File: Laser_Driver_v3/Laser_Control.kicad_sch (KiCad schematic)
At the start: 10 parts, among them U30 74AHCT125, U31 AD9833xRM, U32 AD5064BRUZ, U33 AD9833xRM

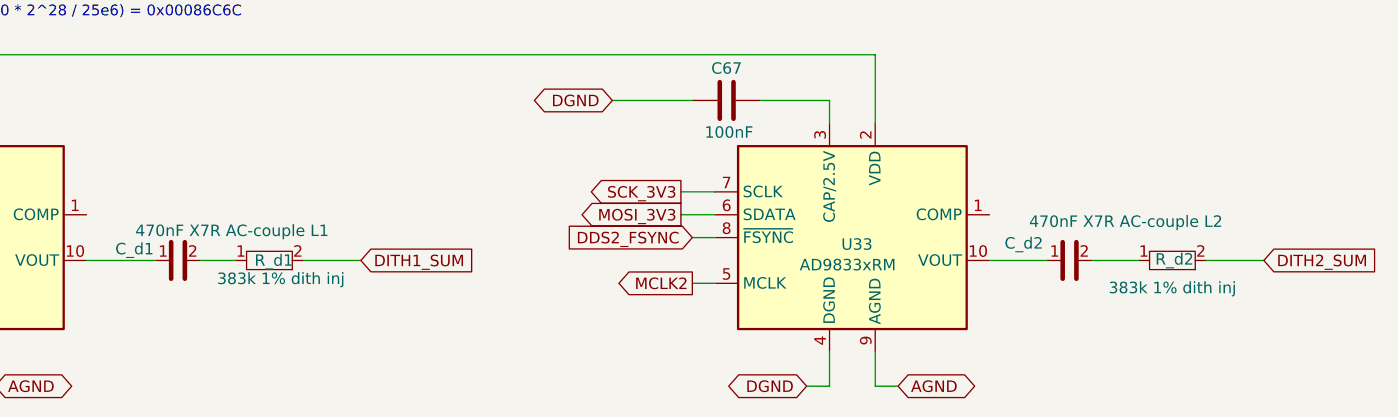
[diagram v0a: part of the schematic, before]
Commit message: Update names, footprints, values, and created BOM
Updated files names, foot prints, component values, parts.
Assigned values from Digikey catalog.
Created CSV BOMs for each schematic.
Including a Power analysis now for all components.
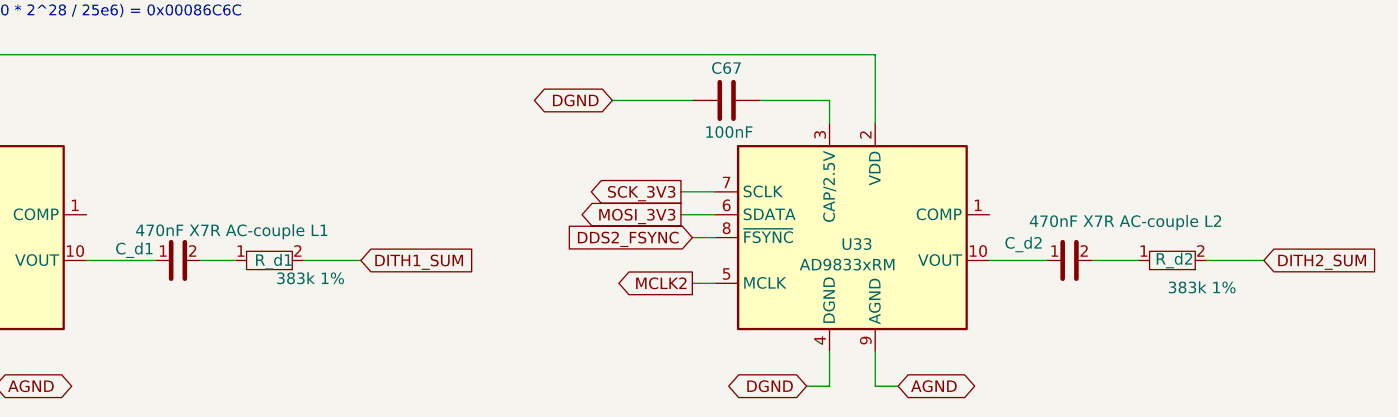
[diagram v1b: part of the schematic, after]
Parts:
- C_d1, C_d2: footprint Capacitor_SMD:C_0805_2012Metric -> Capacitor_SMD:C_0805_2012Metric_Pad1.18x1.45mm_HandSolder
- R_d1, R_d2: value 383k 1% dith inj -> 383k 1%; footprint Resistor_SMD:R_0402_1005Metric -> Resistor_SMD:R_0805_2012Metric_Pad1.20x1.40mm_HandSolder
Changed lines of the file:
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@@
 			)
 		)
-		(property "Footprint" "Capacitor_SMD:C_0805_2012Metric"
+		(property "Footprint" "Capacitor_SMD:C_0805_2012Metric_Pad1.18x1.45mm_HandSolder"
 			(at 86.36 143.51 0)
 			(hide yes)
@@
 			)
 		)
-		(property "Footprint" "Capacitor_SMD:C_0805_2012Metric"
+		(property "Footprint" "Capacitor_SMD:C_0805_2012Metric_Pad1.18x1.45mm_HandSolder"
 			(at 185.42 143.51 0)
 			(hide yes)
@@
 			)
 		)
-		(property "Value" "383k 1% dith inj"
+		(property "Value" "383k 1%"
 			(at 203.962 146.558 90)
 			(show_name no)
@@
 			)
 		)
-		(property "Footprint" "Resistor_SMD:R_0402_1005Metric"
+		(property "Footprint" "Resistor_SMD:R_0805_2012Metric_Pad1.20x1.40mm_HandSolder"
 			(at 196.85 143.51 0)
 			(hide yes)
@@
 			)
 		)
-		(property "Value" "383k 1% dith inj"
+		(property "Value" "383k 1%"
 			(at 104.902 145.542 90)
 			(show_name no)
@@
 			)
 		)
-		(property "Footprint" "Resistor_SMD:R_0402_1005Metric"
+		(property "Footprint" "Resistor_SMD:R_0805_2012Metric_Pad1.20x1.40mm_HandSolder"
 			(at 96.52 143.51 0)
 			(hide yes)

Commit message: Clearing ERC errors. laying out components.
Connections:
- no-connect marks 1 -> 3
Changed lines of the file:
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@@
+	)
+	(no_connect
+		(at 176.53 138.43)
 	)
 	(no_connect
 		(at 111.76 73.66)
 	)
+	(no_connect
+		(at 76.2 138.43)
+	)
 	(wire
 		(pts
@@
 	(wire
 		(pts
+			(xy 40.64 163.83) (xy 40.64 168.91)
+		)
+		(stroke
+			(width 0)
+			(type default)
+		)
+	)
+	(wire
+		(pts
 			(xy 44.45 62.23) (xy 44.45 43.18)
 		)
@@
 	(wire
 		(pts
+			(xy 29.21 91.44) (xy 36.83 91.44)
+		)
+		(stroke
+			(width 0)
+			(type default)
+		)
+	)
+	(wire
+		(pts
 			(xy 111.76 66.04) (xy 119.38 66.04)
 		)
@@
 	(wire
 		(pts
-			(xy 29.21 91.44) (xy 36.83 91.44)
-		)
-		(stroke
-			(width 0)
-			(type default)
-		)
-	)
-	(wire
-		(pts
 			(xy 66.04 59.69) (xy 69.85 59.69)
 		)
@@
 		(pts
 			(xy 30.48 59.69) (xy 50.8 59.69)
+		)
+		(stroke
+			(width 0)
+			(type default)
+		)
+	)
+	(wire
+		(pts
+			(xy 35.56 163.83) (xy 40.64 163.83)
 		)
 		(stroke
@@
 	)
 	(global_label "DGND"
-		(shape bidirectional)
+		(shape output)
 		(at 55.88 157.48 180)
 		(fields_autoplaced yes)
@@
 		)
 		(property "Intersheetrefs" "${INTERSHEET_REFS}"
-			(at 46.643 157.48 0)
+			(at 47.7543 157.48 0)
 			(hide yes)
 			(show_name no)
@@
 	)
 	(global_label "DGND"
-		(shape bidirectional)
+		(shape output)
 		(at 156.21 157.48 180)
 		(fields_autoplaced yes)
@@
 		)
 		(property "Intersheetrefs" "${INTERSHEET_REFS}"
-			(at 146.973 157.48 0)
+			(at 148.0843 157.48 0)
 			(hide yes)
 			(show_name no)
@@
 	)
 	(global_label "AGND"
-		(shape bidirectional)
+		(shape output)
 		(at 166.37 157.48 0)
 		(fields_autoplaced yes)
@@
 		)
 		(property "Intersheetrefs" "${INTERSHEET_REFS}"
-			(at 175.4256 157.48 0)
+			(at 174.3143 157.48 0)
 			(hide yes)
 			(show_name no)
@@
 		)
 	)
+	(global_label "DGND"
+		(shape input)
+		(at 35.56 163.83 180)
+		(fields_autoplaced yes)
+		(effects
+			(font
+				(size 1.27 1.27)
+			)
+			(justify right)
+		)
+		(property "Intersheetrefs" "${INTERSHEET_REFS}"
+			(at 27.4343 163.83 0)
+			(hide yes)
+			(show_name no)
+			(do_not_autoplace no)
+			(effects
+				(font
+					(size 1.27 1.27)
+				)
+				(justify right)
+			)
+		)
+	)
 	(global_label "DDS2_FSYNC"
 		(shape input)
@@
 	)
 	(global_label "AGND"
-		(shape bidirectional)
+		(shape input)
 		(at 29.21 91.44 180)
 		(fields_autoplaced yes)
@@
 		)
 		(property "Intersheetrefs" "${INTERSHEET_REFS}"
-			(at 20.1544 91.44 0)
+			(at 21.2657 91.44 0)
 			(hide yes)
 			(show_name no)
@@
 	)
 	(global_label "AGND"
-		(shape bidirectional)
+		(shape output)
 		(at 66.04 157.48 0)
 		(fields_autoplaced yes)
@@
 		)
 		(property "Intersheetrefs" "${INTERSHEET_REFS}"
-			(at 75.0956 157.48 0)
+			(at 73.9843 157.48 0)
 			(hide yes)
 			(show_name no)
@@
 	)
 	(symbol
+		(lib_name "AD9833xRM_1")
 		(lib_id "Interface:AD9833xRM")
 		(at 60.96 140.97 0)
@@
 		)
 		(property "Value" "383k 1%"
-			(at 104.902 145.542 90)
+			(at 99.314 146.558 90)
 			(show_name no)
 			(do_not_autoplace no)
@@
 		(property "Datasheet" ""
 			(at 96.52 143.51 0)
+			(hide yes)
 			(show_name no)
 			(do_not_autoplace no)
@@
 					(unit 1)
 				)
+			)
+		)
+	)
+	(symbol
+		(lib_id "power:GND")
+		(at 40.64 168.91 0)
+		(unit 1)
+		(body_style 1)
+		(exclude_from_sim no)
+		(in_bom yes)
+		(on_board yes)
+		(in_pos_files yes)
+		(dnp no)
+		(property "Reference" "#PWR032"
+			(at 40.64 175.26 0)
+			(hide yes)
+			(show_name no)
+			(do_not_autoplace no)
+			(effects
+				(font
+					(size 1.27 1.27)
+				)
+			)
+		)
+		(property "Value" "DGND"
+			(at 42.672 169.418 0)
+			(show_name no)
+			(do_not_autoplace no)
+			(effects
+				(font
+					(size 1.27 1.27)
+				)
+			)
+		)
+		(property "Footprint" ""
+			(at 40.64 168.91 0)
+			(hide yes)
+			(show_name no)
+			(do_not_autoplace no)
+			(effects
+				(font
+					(size 1.27 1.27)
+				)
+			)
+		)
+		(property "Datasheet" ""
+			(at 40.64 168.91 0)
+			(hide yes)
+			(show_name no)
+			(do_not_autoplace no)
+			(effects
+				(font
+					(size 1.27 1.27)
+				)
+			)
+		)
+		(property "Description" "Power symbol creates a global label with name \"GND\" , ground"
+			(at 40.64 168.91 0)
+			(hide yes)
+			(show_name no)
+			(do_not_autoplace no)
+			(effects
+				(font
+					(size 1.27 1.27)
+				)
+			)
+		)
+		(pin "1"
+		)
+		(instances
+			(project "laser_driver_v3"
+				(path "/b2c3d4e5-f6a7-8901-bcde-f12345678901/e4d7b089-62e9-414f-b4cc-abd1480c07cf"
+					(reference "#PWR032")
+					(unit 1)
+				)

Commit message: Added display to schematic.  Updated BOM.
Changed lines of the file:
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@@
 	)
 	(global_label "DDS2_FSYNC"
-		(shape input)
+		(shape output)
 		(at 143.51 140.97 180)
 		(fields_autoplaced yes)
@@
 		)
 		(property "Intersheetrefs" "${INTERSHEET_REFS}"
-			(at 143.51 140.97 0)
+			(at 128.611 140.97 0)
 			(hide yes)
 			(show_name no)

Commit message: Update to teensy pinout and config. Working on PCB
Improved pin selection on Teensy for better operation.
Started working through the PCB from in the power input.
Updating footprints and getting the layout organized.
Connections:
- net 5V_DAC: no longer U32.9 (~{CLR})
- net GND: no longer U30.11 (4Y), U30.12 (4A)
- new net: U30.11 (4Y), U32.9 (~{CLR})
- new net AD5064_CLR: U30.12 (4A)
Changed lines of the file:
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@@
-	)
-	(junction
-		(at 69.85 67.31)
-		(diameter 0)
-		(color 0 0 0 0)
 	)
 	(junction
@@
 	)
 	(junction
-		(at 69.85 64.77)
-		(diameter 0)
-		(color 0 0 0 0)
-	)
-	(junction
 		(at 69.85 57.15)
-		(diameter 0)
-		(color 0 0 0 0)
-	)
-	(junction
-		(at 95.25 63.5)
 		(diameter 0)
 		(color 0 0 0 0)
@@
 	(wire
 		(pts
-			(xy 69.85 67.31) (xy 71.12 67.31)
+			(xy 66.04 67.31) (xy 71.12 67.31)
 		)
 		(stroke
@@
 	(wire
 		(pts
+			(xy 76.2 86.36) (xy 76.2 64.77)
+		)
+		(stroke
+			(width 0)
+			(type default)
+		)
+	)
+	(wire
+		(pts
 			(xy 50.8 64.77) (xy 48.26 64.77)
 		)
@@
 	(wire
 		(pts
-			(xy 69.85 46.99) (xy 73.66 46.99)
-		)
-		(stroke
-			(width 0)
-			(type default)
-		)
-	)
-	(wire
-		(pts
-			(xy 80.01 86.36) (xy 80.01 62.23)
+			(xy 72.39 53.34) (xy 73.66 53.34)
 		)
 		(stroke
@@
 	(wire
 		(pts
-			(xy 95.25 62.23) (xy 95.25 63.5)
-		)
-		(stroke
-			(width 0)
-			(type default)
-		)
-	)
-	(wire
-		(pts
 			(xy 143.51 146.05) (xy 146.05 146.05)
 		)
@@
 	(wire
 		(pts
-			(xy 73.66 46.99) (xy 73.66 57.15)
-		)
-		(stroke
-			(width 0)
-			(type default)
-		)
-	)
-	(wire
-		(pts
-			(xy 80.01 62.23) (xy 95.25 62.23)
+			(xy 73.66 53.34) (xy 73.66 57.15)
+		)
+		(stroke
+			(width 0)
+			(type default)
+		)
+	)
+	(wire
+		(pts
+			(xy 74.93 46.99) (xy 74.93 62.23)
 		)
 		(stroke
@@
 	(wire
 		(pts
-			(xy 69.85 64.77) (xy 69.85 67.31)
-		)
-		(stroke
-			(width 0)
-			(type default)
-		)
-	)
-	(wire
-		(pts
 			(xy 114.3 43.18) (xy 114.3 58.42)
 		)
@@
 	(wire
 		(pts
-			(xy 66.04 67.31) (xy 69.85 67.31)
-		)
-		(stroke
-			(width 0)
-			(type default)
-		)
-	)
-	(wire
-		(pts
 			(xy 73.66 57.15) (xy 69.85 57.15)
 		)
@@
 	(wire
 		(pts
-			(xy 66.04 62.23) (xy 69.85 62.23)
+			(xy 66.04 62.23) (xy 74.93 62.23)
 		)
 		(stroke
@@
 	(wire
 		(pts
-			(xy 69.85 62.23) (xy 69.85 64.77)
-		)
-		(stroke
-			(width 0)
-			(type default)
-		)
-	)
-	(wire
-		(pts
 			(xy 35.56 135.89) (xy 45.72 135.89)
 		)
@@
 	(wire
 		(pts
-			(xy 95.25 63.5) (xy 96.52 63.5)
+			(xy 71.12 46.99) (xy 74.93 46.99)
+		)
+		(stroke
+			(width 0)
+			(type default)
+		)
+	)
+	(wire
+		(pts
+			(xy 90.17 63.5) (xy 96.52 63.5)
 		)
 		(stroke
@@
 	(wire
 		(pts
-			(xy 90.17 63.5) (xy 95.25 63.5)
-		)
-		(stroke
-			(width 0)
-			(type default)
-		)
-	)
-	(wire
-		(pts
 			(xy 63.5 120.65) (xy 163.83 120.65)
 		)
@@
 	(wire
 		(pts
-			(xy 80.01 86.36) (xy 119.38 86.36)
+			(xy 76.2 86.36) (xy 119.38 86.36)
 		)
 		(stroke
@@
 	(wire
 		(pts
-			(xy 66.04 64.77) (xy 69.85 64.77)
+			(xy 66.04 64.77) (xy 76.2 64.77)
 		)
 		(stroke
@@
 		)
 	)
+	(global_label "AD5064_CLR"
+		(shape output)
+		(at 71.12 46.99 180)
+		(fields_autoplaced yes)
+		(effects
+			(font
+				(size 1.27 1.27)
+			)
+			(justify right)
+		)
+		(property "Intersheetrefs" "${INTERSHEET_REFS}"
+			(at 56.4025 46.99 0)
+			(hide yes)
+			(show_name no)
+			(do_not_autoplace no)
+			(effects
+				(font
+					(size 1.27 1.27)
+				)
+				(justify right)
+			)
+		)
+	)
 	(global_label "3V3"
 		(shape output)
@@
 	(global_label "5V_DAC"
 		(shape output)
-		(at 69.85 46.99 180)
-		(fields_autoplaced yes)
-		(effects
-			(font
-				(size 1.27 1.27)
-			)
-			(justify right)
-		)
-		(property "Intersheetrefs" "${INTERSHEET_REFS}"
-			(at 59.9705 46.99 0)
-			(hide yes)
-			(show_name no)
+		(at 72.39 53.34 180)
+		(fields_autoplaced yes)
+		(effects
+			(font
+				(size 1.27 1.27)
+			)
+			(justify right)
+		)
+		(property "Intersheetrefs" "${INTERSHEET_REFS}"
+			(at 62.5105 53.34 0)
+			(hide yes)
+			(show_name no)

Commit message: Added separate xfrmer for 6V.
Added inrush protection with NTC and increased capacitance to reduce ripple on 6V
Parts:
- renumbered C66 to C72, C67 to C73
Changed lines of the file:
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@@
 		(in_pos_files yes)
 		(dnp no)
-		(property "Reference" "#PWR027"
+		(property "Reference" "#PWR029"
 			(at 48.26 85.09 0)
 			(hide yes)
@@
 			(project "laser_driver_v3"
 				(path "/b2c3d4e5-f6a7-8901-bcde-f12345678901/e4d7b089-62e9-414f-b4cc-abd1480c07cf"
-					(reference "#PWR027")
+					(reference "#PWR029")
 					(unit 1)
 				)
@@
 		(in_pos_files yes)
 		(dnp no)
-		(property "Reference" "#PWR026"
+		(property "Reference" "#PWR027"
 			(at 36.83 99.06 0)
 			(hide yes)
@@
 			(project "laser_driver_v3"
 				(path "/b2c3d4e5-f6a7-8901-bcde-f12345678901/e4d7b089-62e9-414f-b4cc-abd1480c07cf"
-					(reference "#PWR026")
+					(reference "#PWR027")
 					(unit 1)
 				)
@@
 		(in_pos_files yes)
 		(dnp no)
-		(property "Reference" "#PWR029"
+		(property "Reference" "#PWR031"
 			(at 83.82 83.82 0)
 			(hide yes)
@@
 			(project "laser_driver_v3"
 				(path "/b2c3d4e5-f6a7-8901-bcde-f12345678901/e4d7b089-62e9-414f-b4cc-abd1480c07cf"
-					(reference "#PWR029")
+					(reference "#PWR031")
 					(unit 1)
 				)
@@
 		(in_pos_files yes)
 		(dnp no)
-		(property "Reference" "#PWR031"
+		(property "Reference" "#PWR033"
 			(at 130.81 69.85 0)
 			(hide yes)
@@
 			(project "laser_driver_v3"
 				(path "/b2c3d4e5-f6a7-8901-bcde-f12345678901/e4d7b089-62e9-414f-b4cc-abd1480c07cf"
-					(reference "#PWR031")
+					(reference "#PWR033")
 					(unit 1)
 				)
@@
 		(in_pos_files yes)
 		(dnp no)
-		(property "Reference" "#PWR028"
+		(property "Reference" "#PWR030"
 			(at 71.12 73.66 0)
 			(hide yes)
@@
 			(project "laser_driver_v3"
 				(path "/b2c3d4e5-f6a7-8901-bcde-f12345678901/e4d7b089-62e9-414f-b4cc-abd1480c07cf"
-					(reference "#PWR028")
+					(reference "#PWR030")
 					(unit 1)
 				)
@@
 		(in_pos_files yes)
 		(dnp no)
-		(property "Reference" "C67"
+		(property "Reference" "C73"
 			(at 147.32 122.174 90)
 			(show_name no)
@@
 			(project "laser_driver_v3"
 				(path "/b2c3d4e5-f6a7-8901-bcde-f12345678901/e4d7b089-62e9-414f-b4cc-abd1480c07cf"
-					(reference "C67")
+					(reference "C73")
 					(unit 1)
 				)
@@
 		(in_pos_files yes)
 		(dnp no)
-		(property "Reference" "#PWR032"
+		(property "Reference" "#PWR028"
 			(at 40.64 175.26 0)
 			(hide yes)
@@
 			(project "laser_driver_v3"
 				(path "/b2c3d4e5-f6a7-8901-bcde-f12345678901/e4d7b089-62e9-414f-b4cc-abd1480c07cf"
-					(reference "#PWR032")
+					(reference "#PWR028")
 					(unit 1)
 				)
@@
 		(in_pos_files yes)
 		(dnp no)
-		(property "Reference" "C66"
+		(property "Reference" "C72"
 			(at 46.99 122.174 90)
 			(show_name no)
@@
 			(project "laser_driver_v3"
 				(path "/b2c3d4e5-f6a7-8901-bcde-f12345678901/e4d7b089-62e9-414f-b4cc-abd1480c07cf"
-					(reference "C66")
+					(reference "C72")
 					(unit 1)
 				)
@@
 		(in_pos_files yes)
 		(dnp no)
-		(property "Reference" "#PWR030"
+		(property "Reference" "#PWR032"
 			(at 86.36 59.69 0)
 			(hide yes)
@@
 			(project "laser_driver_v3"
 				(path "/b2c3d4e5-f6a7-8901-bcde-f12345678901/e4d7b089-62e9-414f-b4cc-abd1480c07cf"
-					(reference "#PWR030")
-					(unit 1)
-				)
+					(reference "#PWR032")
+					(unit 1)
+				)
